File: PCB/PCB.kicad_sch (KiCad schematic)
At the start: 0 parts

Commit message: added journal entry #2, started schematic
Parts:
- added C1: 1uF, symbol Device:C
- added C2, C3, C5, C7: 10uF, symbol Device:C
- added C4: C, symbol Device:C
- added C6: 10uf, symbol Device:C
- added C8: 0.1uF, symbol Device:C
- added J1: USB_C_Receptacle_USB2.0_16P, symbol Connector:USB_C_Receptacle_USB2.0_16P
- added L1: 2.2uH, symbol Device:L
- added NTC: 10k, symbol Device:Thermistor_NTC
- added R1, R2: 5.1k, symbol Device:R
- added R3, R4: 22, symbol Device:R
- added R5: 100, symbol Device:R
- added R6: 3k, symbol Device:R
- added R7: 3.09k, symbol Device:R
- added U1: HT-CT62, RF_Module:Heltec_HT-CT62, symbol RF_Module:HT-CT62
- added U2: SAM-M10Q, RF_GPS:ublox_SAM-M8Q, symbol RF_GPS:SAM-M8Q
- added U3: ER_OLEDM0.91_1x-I2C, Display:ER_OLEDM0.91_1x-I2C, symbol Display_Graphic:ER_OLEDM0.91_1x-I2C
- added U4: TPS63001, Package_SON:Texas_DRC0010J_ThermalVias, symbol Regulator_Switching:TPS63001
- added U5: TPS22917DBV, Package_TO_SOT_SMD:SOT-23-6, symbol Power_Management:TPS22917DBV
- added U6: BQ24074RGT, Package_DFN_QFN:VQFN-16-1EP_3x3mm_P0.5mm_EP1.6x1.6mm, symbol Battery_Management:BQ24074RGT
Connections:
- new net: R6.2, U6.16 (ISET)
- new net: R7.2, U6.12 (ILIM)
- new net: NTC.1, U6.1 (TS)
- new net: J1.A5 (CC1), R1.1
- new net: J1.B5 (CC2), R2.1
- new net: R3.1, U1.17 (GPIO18_DN)
- new net: R4.1, U1.18 (GPIO19_DP)
- new net: L1.1, U4.2 (L2)
- new net: L1.2, U4.4 (L1)
- new net +3V3: C5.1, C7.1, U1.12 (VDD), U4.1 (VOUT), U4.10 (FB)
- new net +BATT: C3.1, U6.2 (BAT), U6.3 (BAT)
- new net GND: C1.1, C2.2, C3.2, C5.2, C6.2, C7.2, C8.1, C8.2, J1.A1 (GND), J1.A12 (GND), J1.B1 (GND), J1.B12 (GND), J1.SH (SHIELD), NTC.2, R1.2, R2.2, R5.2, R6.1, R7.1, U1.13 (GND), U1.2 (GND), U1.21 (GND), U2.1 (GND), U2.10 (GND), U2.11 (GND), U2.15 (GND), U2.16 (GND), U2.20 (GND), U2.4 (GND), U2.5 (GND), U2.6 (GND), U3.1 (GND), U4.11 (PGND), U4.3 (PGND), U4.6 (EN), U4.7 (PS/SYNC), U4.8 (VINA), U4.9 (GND), U5.2 (GND), U6.17 (VSS), U6.4 (~{CE}), U6.5 (EN2), U6.8 (VSS)
- new net SYS: C2.1, C6.1, R5.1, U4.5 (VIN), U6.10 (OUT), U6.11 (OUT)
- new net USB_D+: J1.A6 (D+), J1.B6 (D+), R4.2
- new net USB_D-: J1.A7 (D-), J1.B7 (D-), R3.2
- new net VBUS_5V: C1.2, J1.A4 (VBUS), J1.A9 (VBUS), J1.B4 (VBUS), J1.B9 (VBUS), U6.13 (IN), U6.6 (EN1)
- no-connect marks 0 -> 5

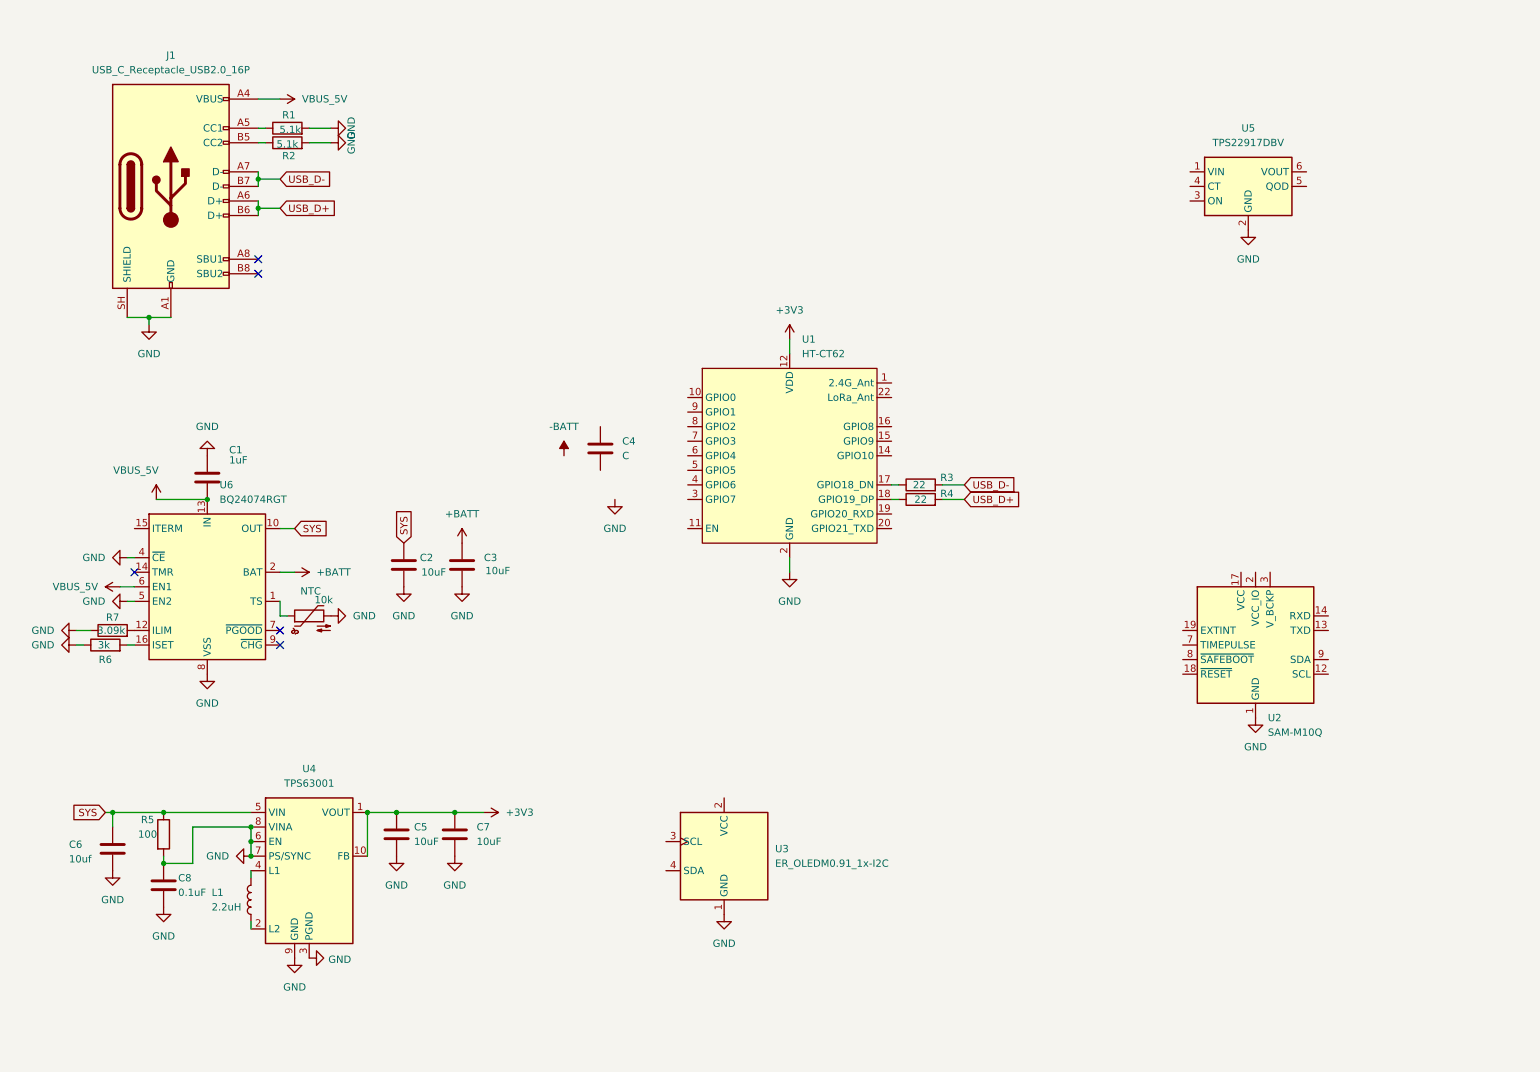
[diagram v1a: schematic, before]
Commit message: added oled screen
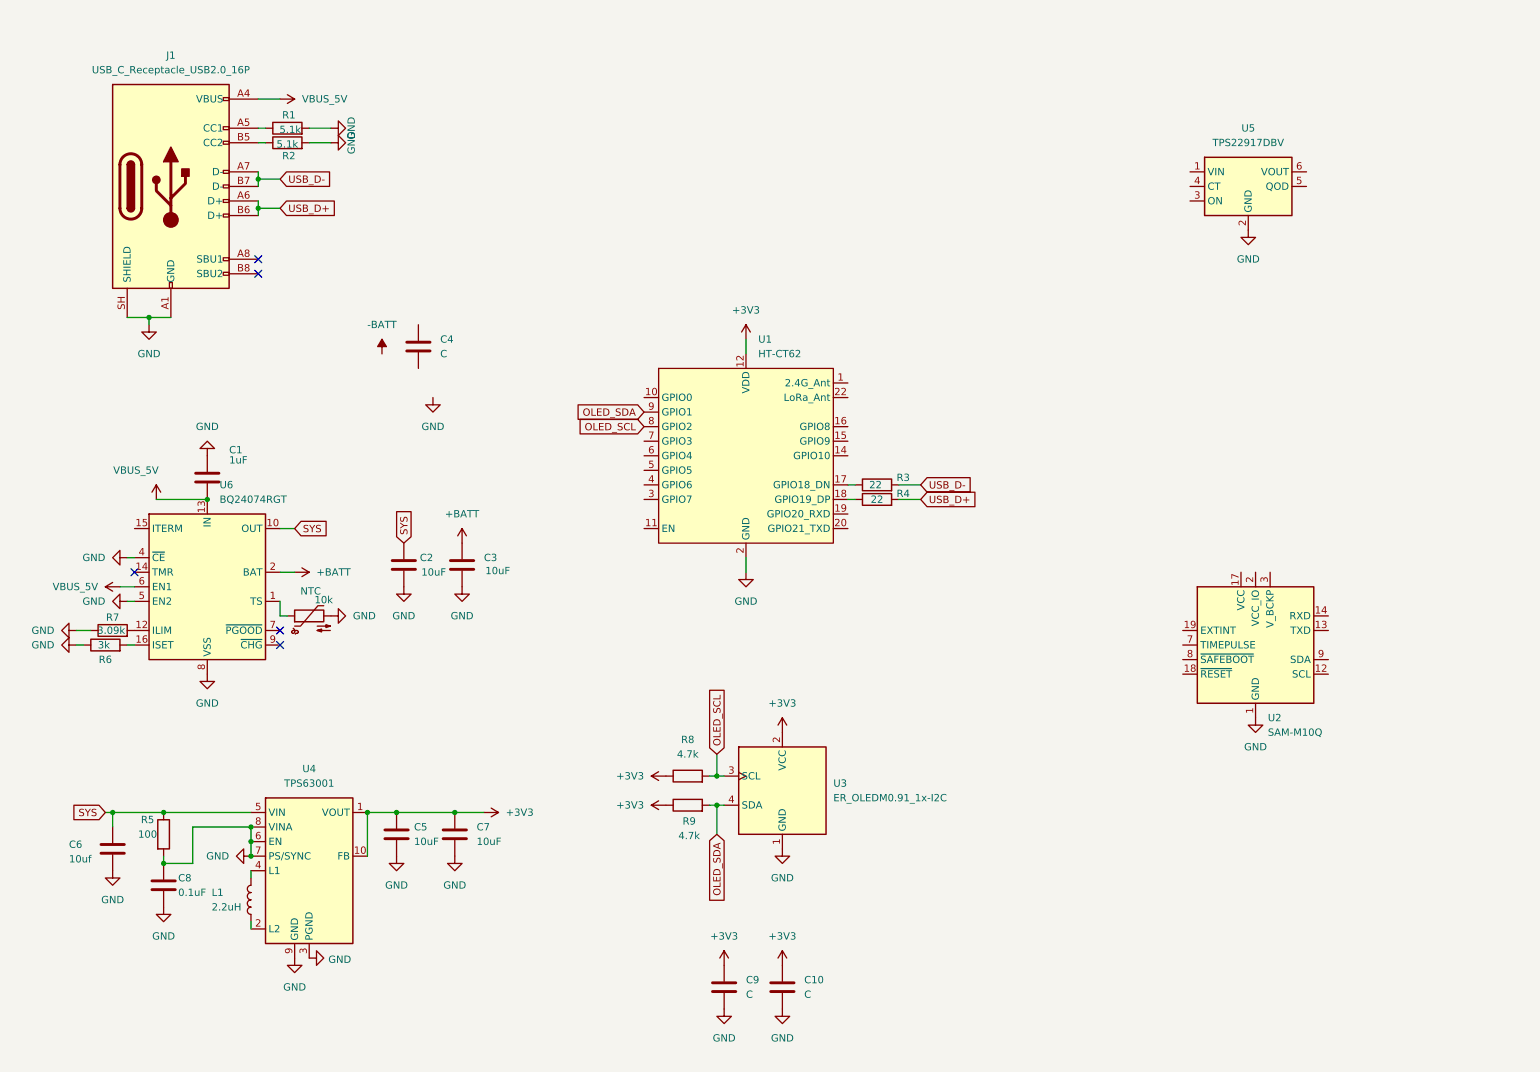
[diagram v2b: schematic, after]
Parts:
- added C10, C9: C, symbol Device:C
- added R8, R9: 4.7k, symbol Device:R
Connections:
- net +3V3: now also U3.2 (VCC), C10.1, C9.1, R8.1, R9.1
- net GND: now also C10.2, C9.2
- net OLED_SCL: now reaches U1.8 (GPIO2)
- net OLED_SCL: now also U3.3 (SCL), R8.2
- net OLED_SDA: now reaches U1.9 (GPIO1)
- net OLED_SDA: now also U3.4 (SDA), R9.2
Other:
- moved on the sheet: C4, R3, R4, U1, U3

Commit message: mapped the ht-ct62
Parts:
- removed C4: C, symbol Device:C
- added C11: 100nF, symbol Device:C
- added C12: 10uF, symbol Device:C
- added C13: 2.2uF, symbol Device:C
- added R10, R11: 10k, symbol Device:R
- added SW1, SW2: SW_Push, symbol Switch:SW_Push
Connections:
- net +3V3: now also C11.2, C12.2, R10.1, R11.1
- net GND: now also C11.1, C12.1, C13.2, SW1.2, SW2.2
- net GNSS_EN: now reaches U5.3 (ON)
- net GNSS_EN: now also U1.10 (GPIO0)
- net GNSS_TX: now reaches U2.13 (TXD)
- net GNSS_TX: now also U1.19 (GPIO20_RXD)
- net GNSS_RX: now reaches U2.14 (RXD)
- net GNSS_RX: now also U1.20 (GPIO21_TXD)
- net at U1.11 (EN): now also C13.1, R10.2, SW1.1
- net at U1.15 (GPIO9): now also R11.2, SW2.1
- no-connect marks 5 -> 14
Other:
- moved on the sheet: C1, C2, C3, NTC, R3, R4, R6, R7, U1, U6

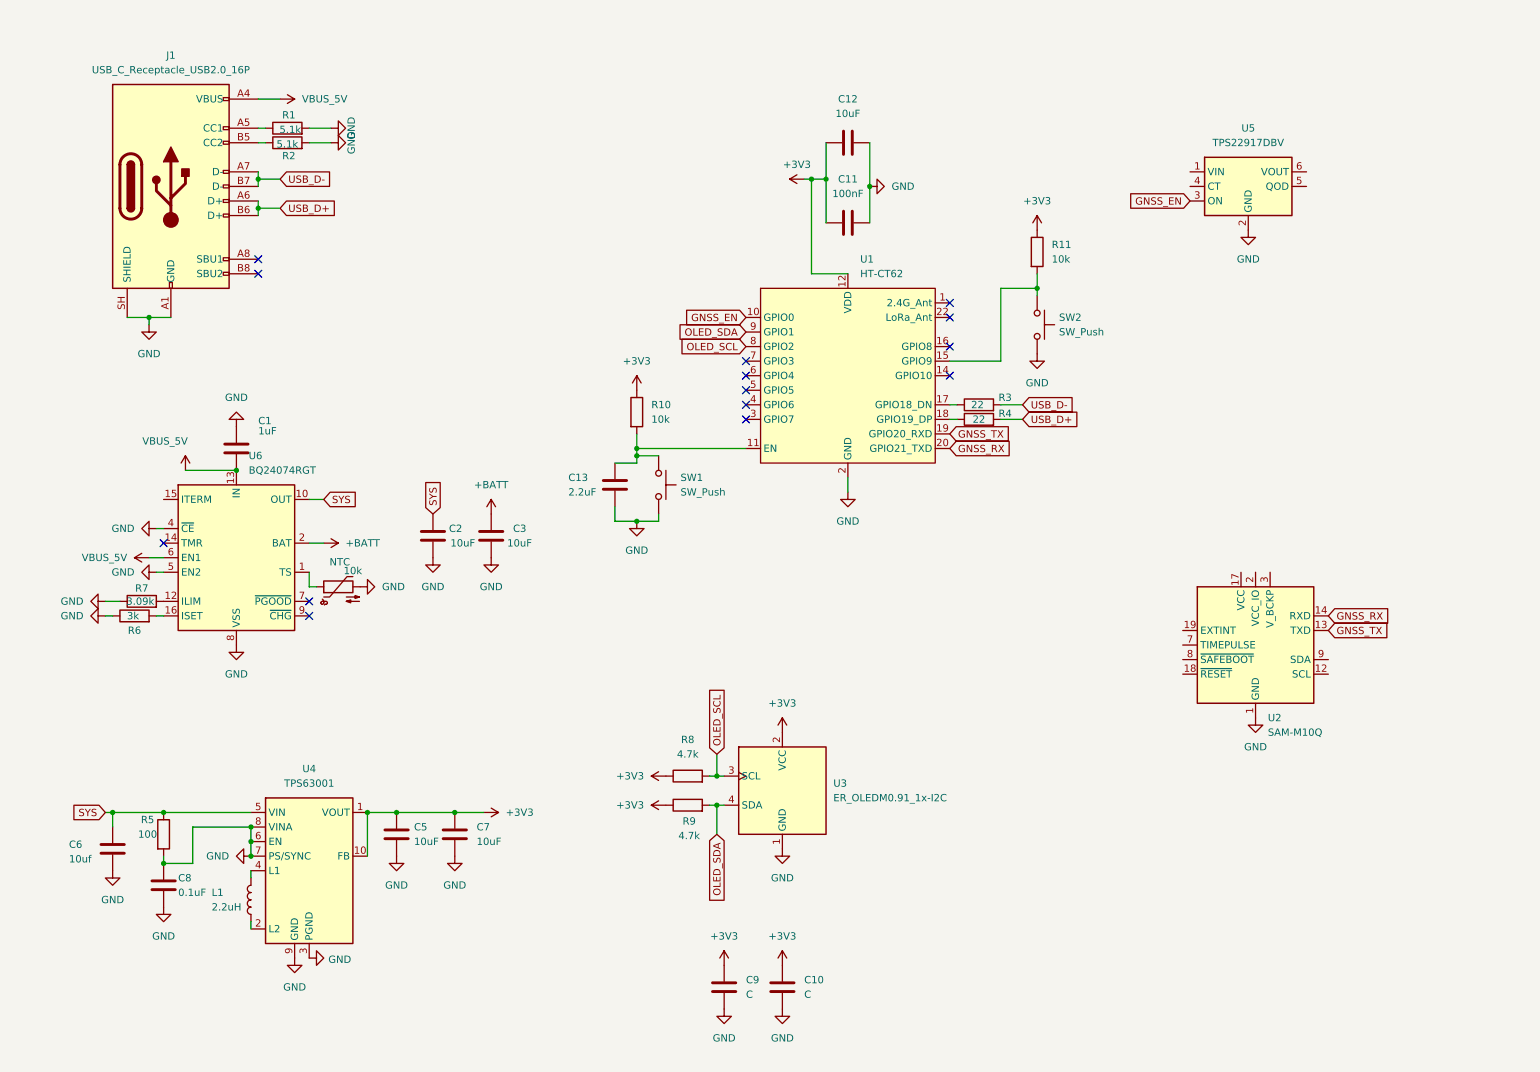
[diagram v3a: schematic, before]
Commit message: mapped the gps and load switch
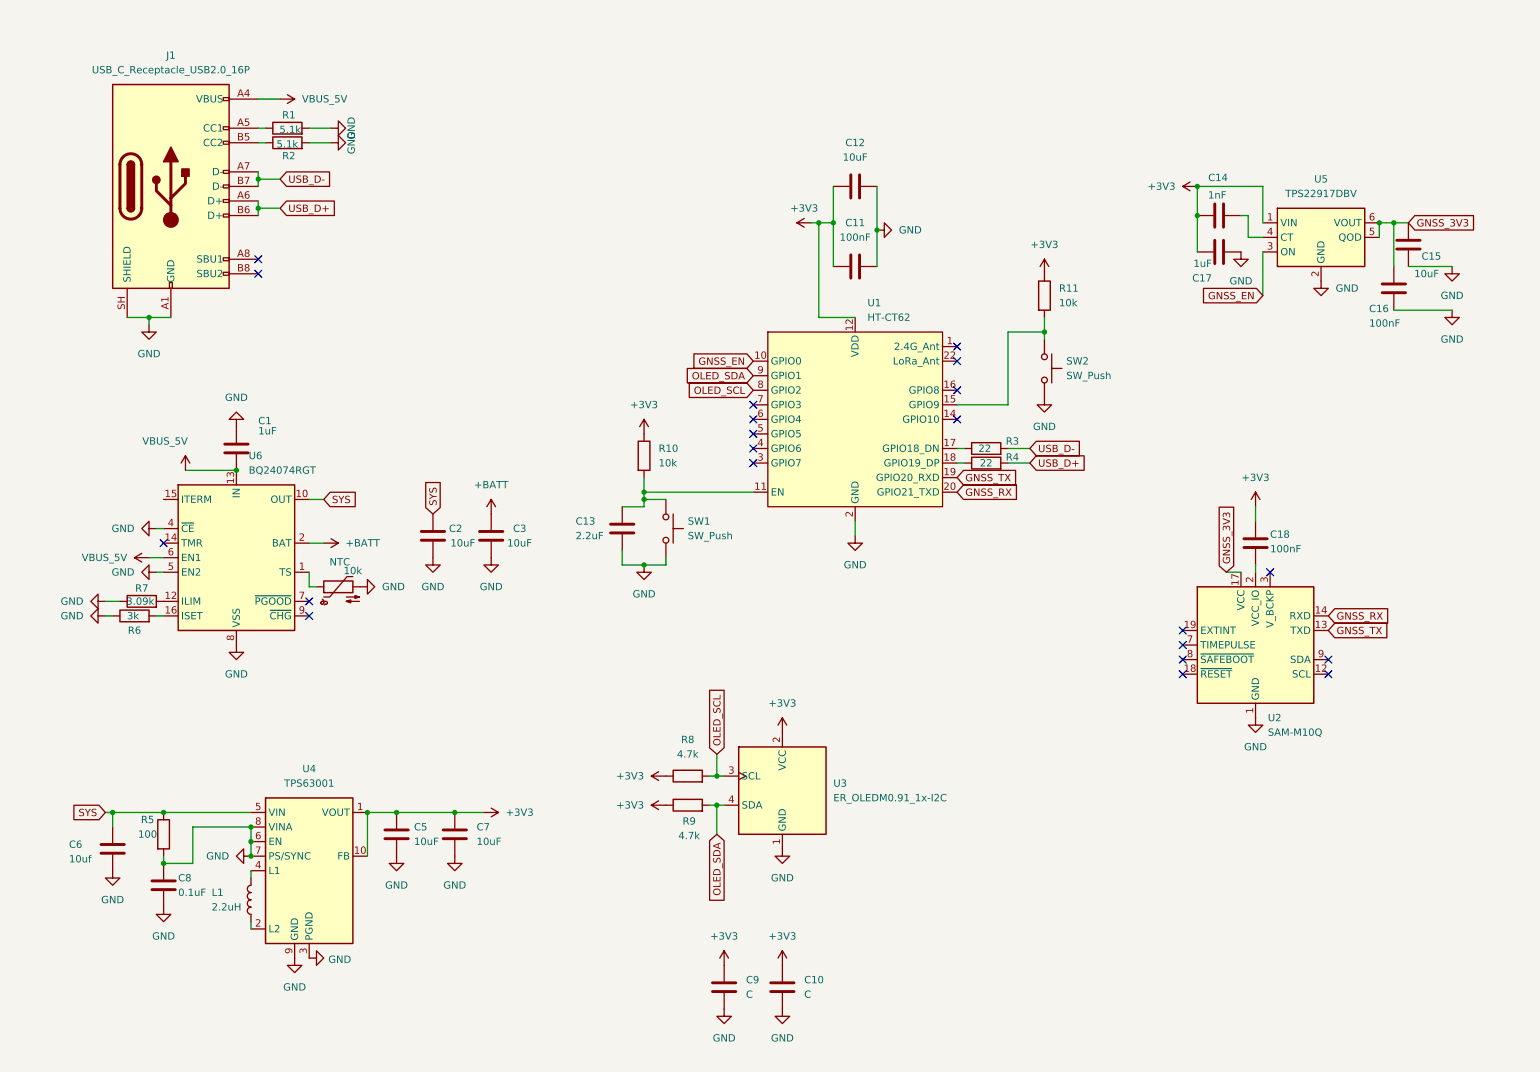
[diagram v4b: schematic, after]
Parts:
- added C14: 1nF, symbol Device:C
- added C15: 10uF, symbol Device:C
- added C16, C18: 100nF, symbol Device:C
- added C17: 1uF, symbol Device:C
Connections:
- net +3V3: now also U5.1 (VIN), C14.1, C17.1, C18.2
- net GND: now also C15.1, C16.1, C17.2
- net at U5.4 (CT): now also C14.2
- net GNSS_3V3: now reaches U5.5 (QOD)
- net GNSS_3V3: now also U2.17 (VCC), U5.6 (VOUT), C15.2, C16.2
- net at U2.2 (VCC_IO): now also C18.1
- no-connect marks 14 -> 21
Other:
- moved on the sheet: C11, C12, C13, R10, R11, R3, R4, SW1, SW2, U1, U5

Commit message: fixing schemating
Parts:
- C10: value C -> 10uF
- C9: value C -> 100nF
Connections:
- net GND: no longer C8.1, R5.2, U4.6 (EN), U4.8 (VINA)
- new net: C8.1, R5.2, U4.6 (EN), U4.8 (VINA)
- no-connect marks 21 -> 22
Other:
- moved on the sheet: C9

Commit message: schematic fix attempts
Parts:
- added J2: 18650_PROTECTED, Connector_JST:JST_PH_B2B-PH-K_1x02_P2.00mm_Vertical, symbol Connector_Generic:Conn_01x02
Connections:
- net +BATT: no longer U6.2 (BAT), U6.3 (BAT)
- new net: U6.2 (BAT), U6.3 (BAT)
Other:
- moved on the sheet: C2, C3, NTC

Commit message: fixing parts of schematic
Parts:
- added C19: 100nF, symbol Device:C
- added R14, R15: 100k, symbol Device:R
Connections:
- net +3V3: now also R10.2, U2.3 (V_BCKP), C19.1; no longer C18.2, R10.1
- net +BATT: now also J2.1 (Pin_1), U6.2 (BAT), U6.3 (BAT), R14.1
- net GND: now also C18.2, J2.2 (Pin_2), C19.2, R15.2
- net GNSS_3V3: now also U2.2 (VCC_IO)
- net at C13.1, SW1.1, U1.11 (EN): now also R10.1; no longer R10.2
- net VBAT_SENSE: now reaches C18.1
- net VBAT_SENSE: now also U1.7 (GPIO3), R14.2, R15.1; no longer U2.2 (VCC_IO)
- no-connect marks 22 -> 20
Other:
- moved on the sheet: C5, C6, C7, C8, J2, L1, R10, R5, U4
